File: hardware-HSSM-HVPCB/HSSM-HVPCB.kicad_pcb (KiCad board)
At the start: 2 copper layers, 66 parts, among them J1 2086-1103, J2 2601-1110, K1 G6DN-1A-L DC12, K2 G6DN-1A-L DC12, Q1 Q_NMOS_SOT-23_IRLML6344, Q2 Q_NMOS_SOT-23_IRLML6344, U1 LNK3204D-TL, U2 CS5480-INZ, U3 LTV-354T, U4 LTV-354T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

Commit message: [#6] Update step models
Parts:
- C2: footprint HSSM-HVPCB:C_Radial_D8_L14_P3.5 -> HSSM-HVPCB:860021374009
- C3: footprint HSSM-HVPCB:C_Radial_D5_L11_P2 -> HSSM-HVPCB:860020372006
- moved RV1 1.43 mm to (130.2, 122.5)
- moved J1 0.34 mm to (166.1, 108.7), turned to 0 degrees
- moved K1 0.17 mm to (155.1, 106.0)
- moved K2 0.17 mm to (155.1, 112.7)

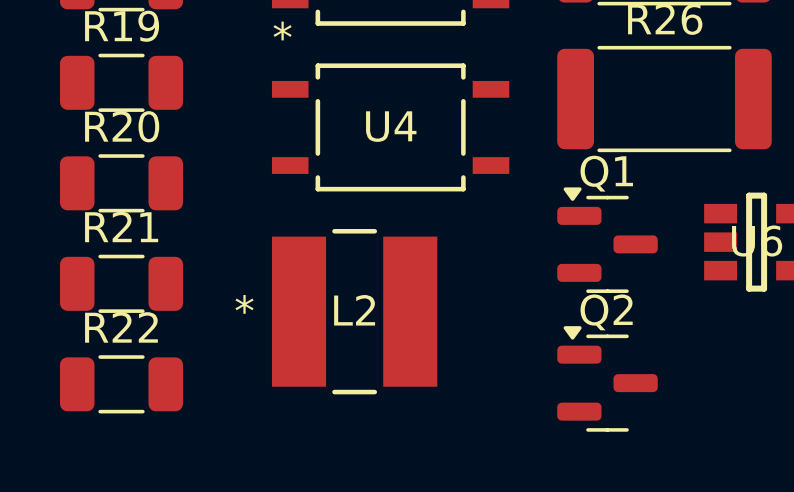
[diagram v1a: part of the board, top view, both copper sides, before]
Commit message: [#6] Add step model for SDR0503-102KL
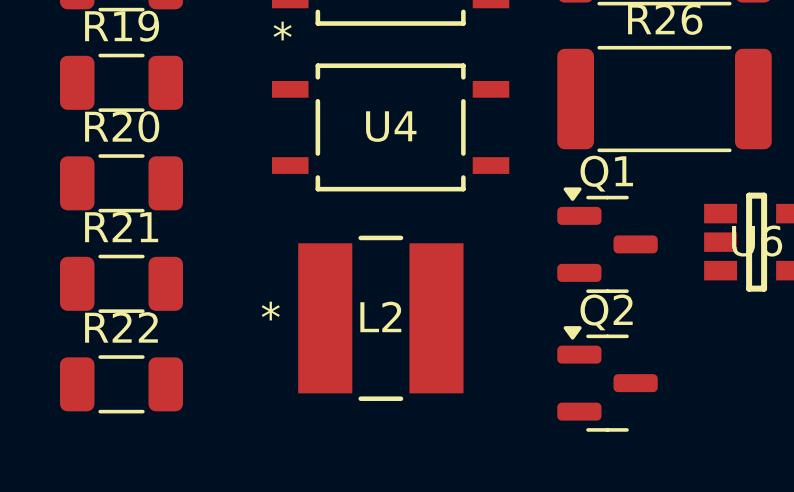
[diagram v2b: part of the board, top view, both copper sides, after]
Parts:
- moved L2 0.90 mm to (109.5, 135.9)

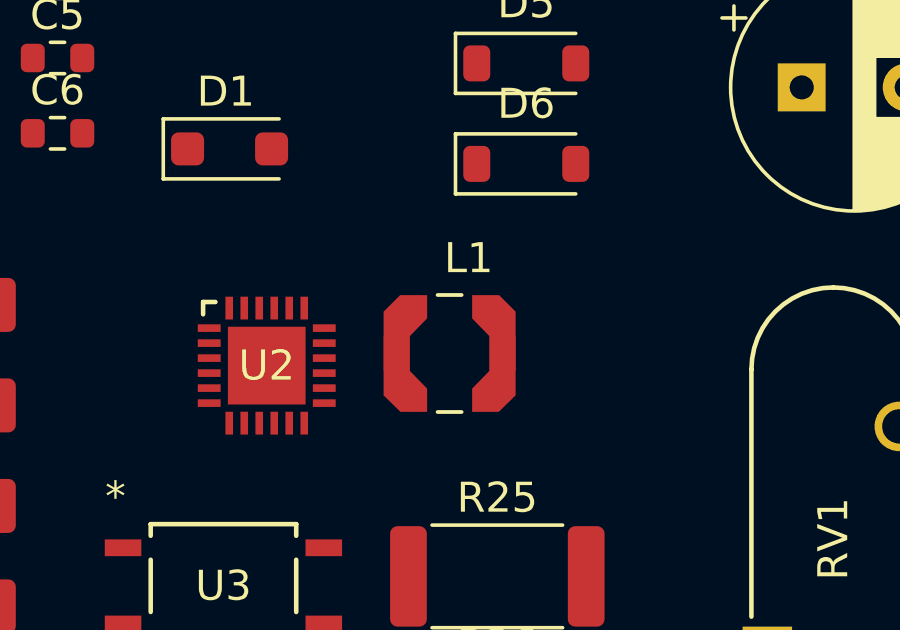
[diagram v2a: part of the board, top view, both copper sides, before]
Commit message: [#6] Add step model for LPS4012-155MRC
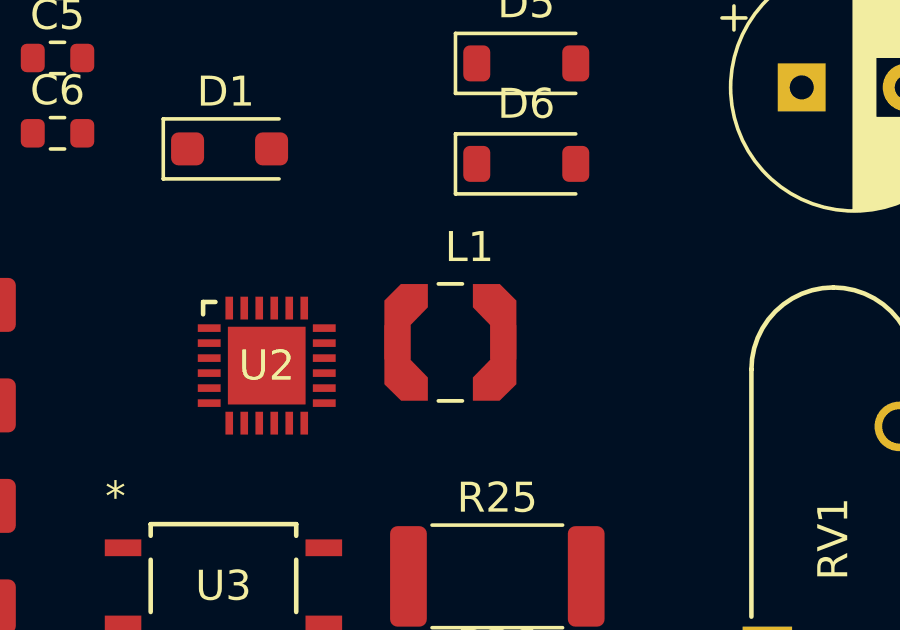
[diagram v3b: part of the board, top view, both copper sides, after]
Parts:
- moved L1 0.37 mm to (117.4, 115.9)

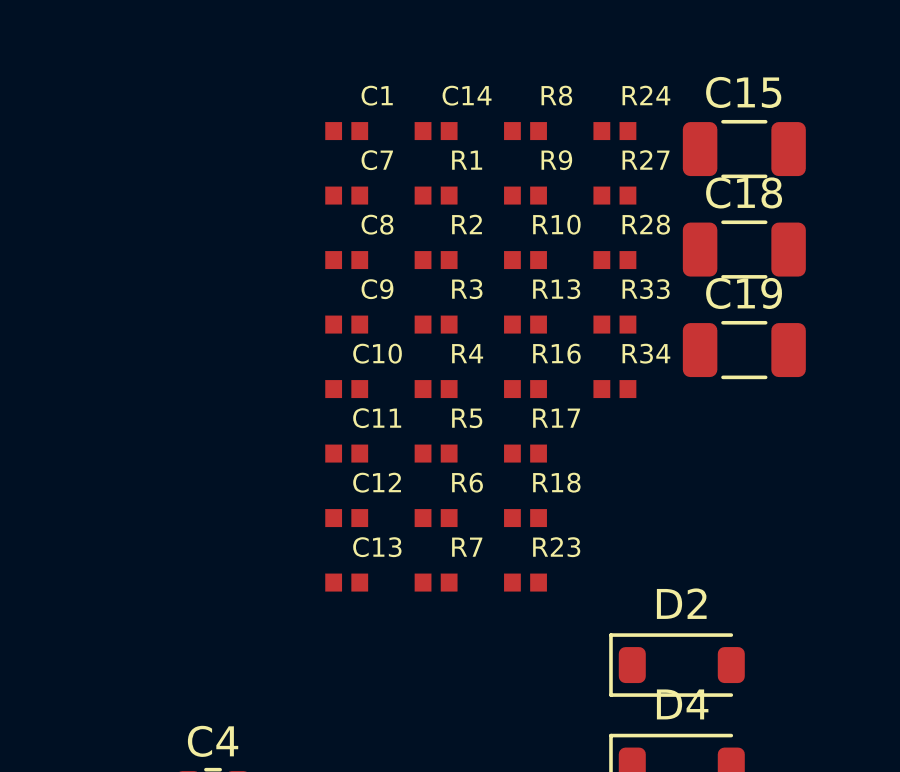
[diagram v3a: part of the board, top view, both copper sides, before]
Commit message: [#6] Add step model R_0402
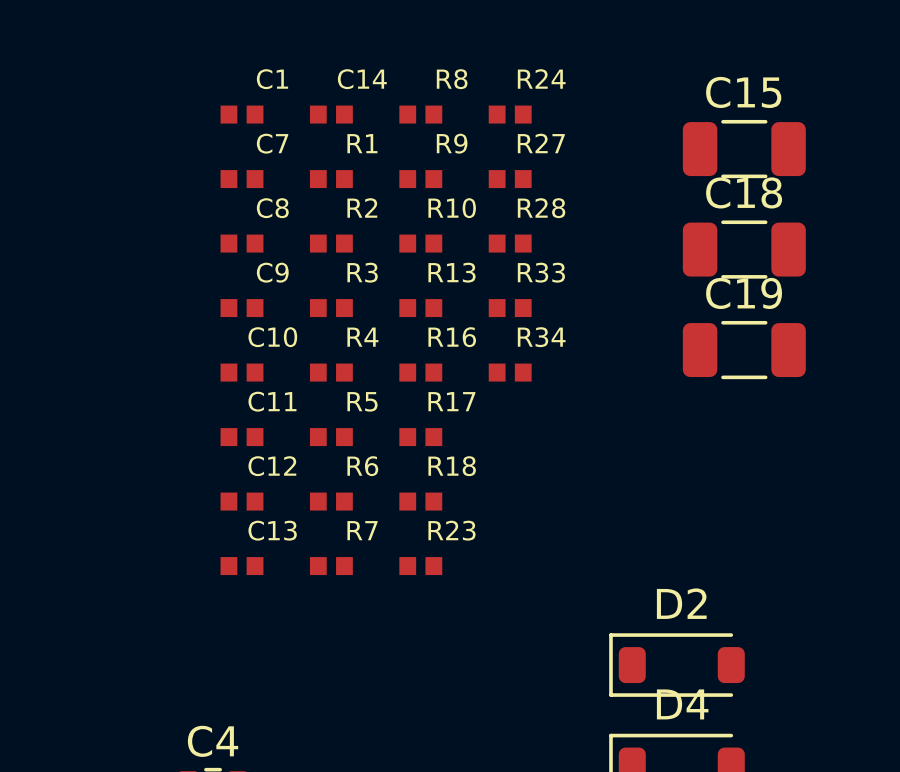
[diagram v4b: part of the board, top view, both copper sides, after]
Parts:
- moved R2 3.53 mm to (108.3, 85.8)
- moved R7 3.53 mm to (108.3, 96.6)
- moved C14 3.53 mm to (108.3, 81.5)
- moved R1 3.53 mm to (108.3, 83.7)
- moved R3 3.53 mm to (108.3, 88.0)
- moved R4 3.53 mm to (108.3, 90.2)
- moved R5 3.53 mm to (108.3, 92.3)
- moved R6 3.53 mm to (108.3, 94.5)
- moved C13 3.53 mm to (105.3, 96.6)
- moved C8 3.53 mm to (105.3, 85.8)
- moved R10 3.53 mm to (111.3, 85.8)
- moved R23 3.53 mm to (111.3, 96.6)
- moved R28 3.53 mm to (114.2, 85.8)
- moved C1 3.53 mm to (105.3, 81.5)
- moved C10 3.53 mm to (105.3, 90.2)
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
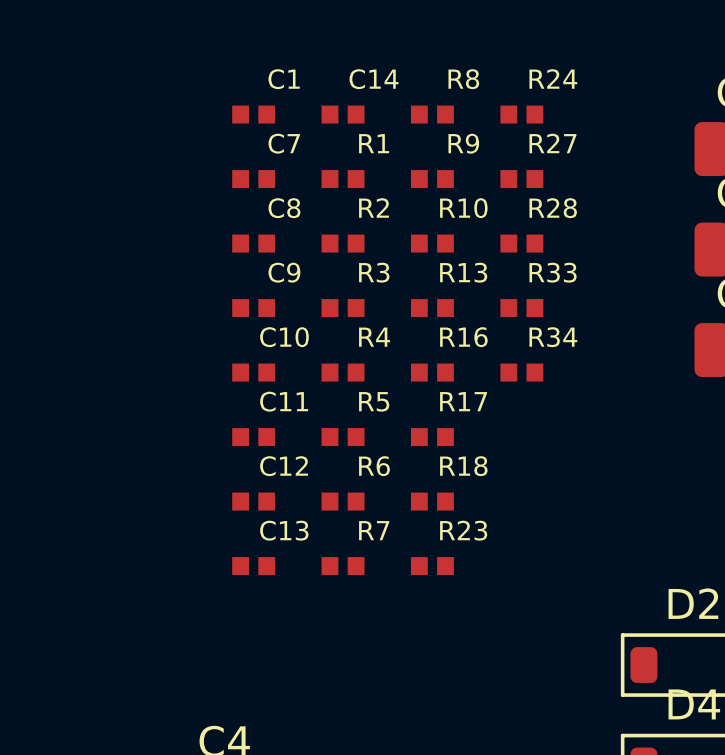
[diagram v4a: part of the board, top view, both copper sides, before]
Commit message: [#6] Add step model C_0402
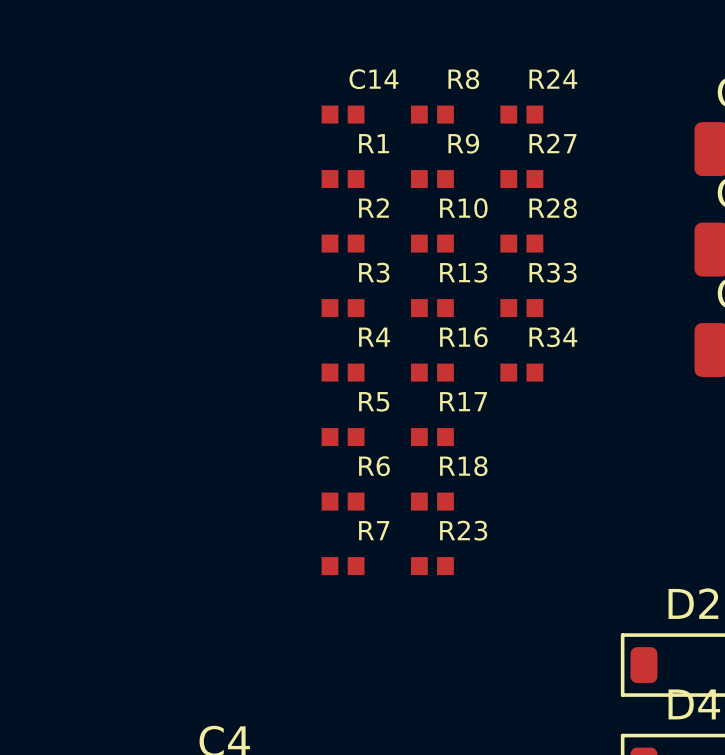
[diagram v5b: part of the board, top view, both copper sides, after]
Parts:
- removed C1: C_0u1_10pct_16V_0402_GRM155R71C104KA88J, HSSM-HVPCB:C_0402
- removed C10, C11, C12, C7, C8, C9: C_33nF_10pct_50V_0402_CC0402KRX7R9BB333, HSSM-HVPCB:C_0402
- removed C13: C_0u1_10pct_50V_0402_GRM155R71H104KE14D, HSSM-HVPCB:C_0402

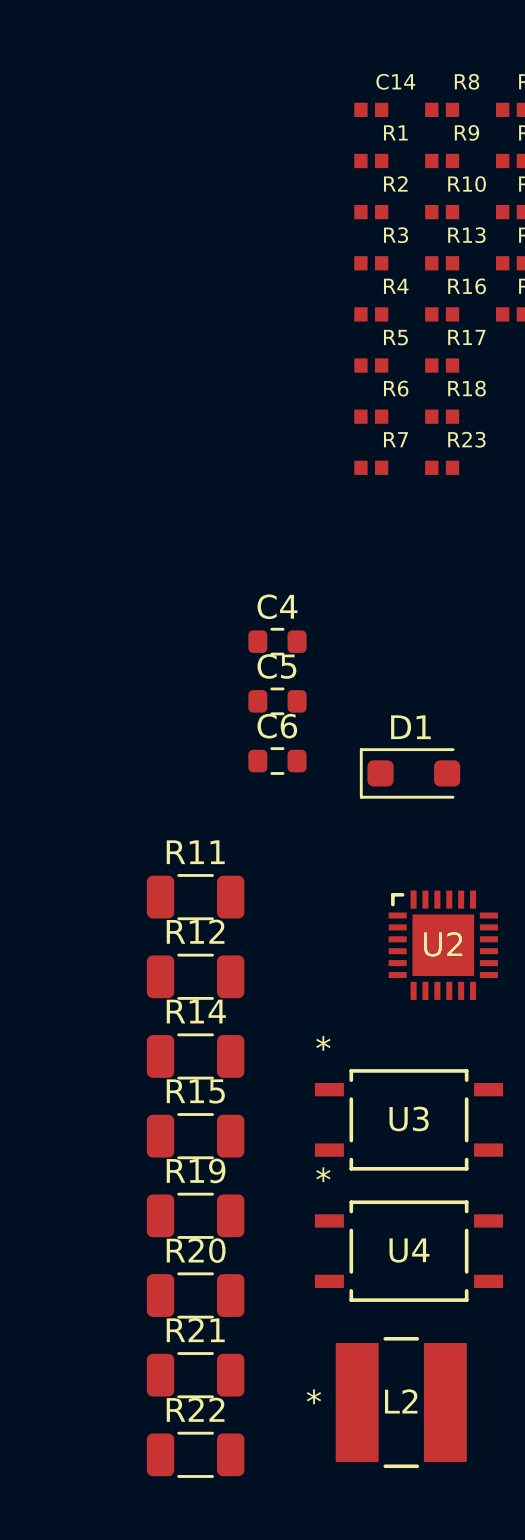
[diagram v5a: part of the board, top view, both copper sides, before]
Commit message: [#6] Fix step model R 1206
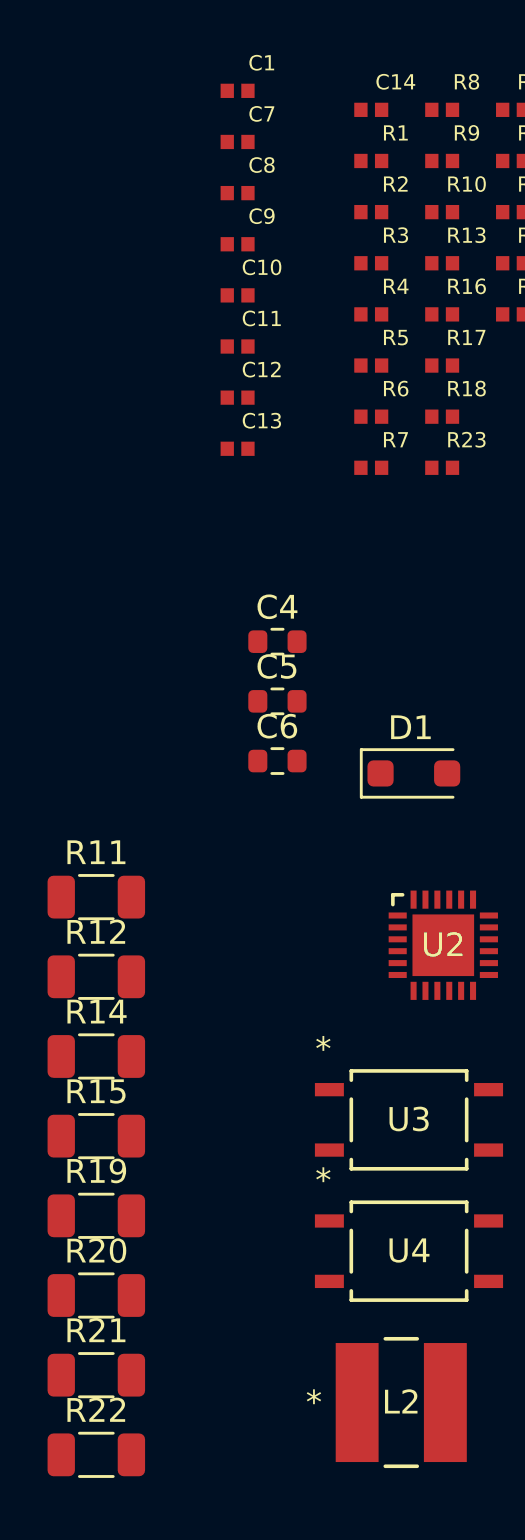
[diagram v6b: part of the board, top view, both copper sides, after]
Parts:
- added C1: C_0u1_10pct_16V_0402_GRM155R71C104KA88J, HSSM-HVPCB:C_0402, F.Cu at (102.7, 80.8)
- added C10: C_33nF_10pct_50V_0402_CC0402KRX7R9BB333, HSSM-HVPCB:C_0402, F.Cu at (102.7, 89.3)
- added C11: C_33nF_10pct_50V_0402_CC0402KRX7R9BB333, HSSM-HVPCB:C_0402, F.Cu at (102.7, 91.5)
- added C12: C_33nF_10pct_50V_0402_CC0402KRX7R9BB333, HSSM-HVPCB:C_0402, F.Cu at (102.7, 93.7)
- added C13: C_0u1_10pct_50V_0402_GRM155R71H104KE14D, HSSM-HVPCB:C_0402, F.Cu at (102.7, 95.8)
- added C7: C_33nF_10pct_50V_0402_CC0402KRX7R9BB333, HSSM-HVPCB:C_0402, F.Cu at (102.7, 82.9)
- added C8: C_33nF_10pct_50V_0402_CC0402KRX7R9BB333, HSSM-HVPCB:C_0402, F.Cu at (102.7, 85.0)
- added C9: C_33nF_10pct_50V_0402_CC0402KRX7R9BB333, HSSM-HVPCB:C_0402, F.Cu at (102.7, 87.2)
- moved R11 4.18 mm to (96.7, 114.7)
- moved R12 4.18 mm to (96.7, 118.0)
- moved R14 4.18 mm to (96.7, 121.3)
- moved R15 4.18 mm to (96.7, 124.7)
- moved R19 4.18 mm to (96.7, 128.1)
- moved R20 4.18 mm to (96.7, 131.4)
- moved R21 4.18 mm to (96.7, 134.8)
- moved R22 4.18 mm to (96.7, 138.1)

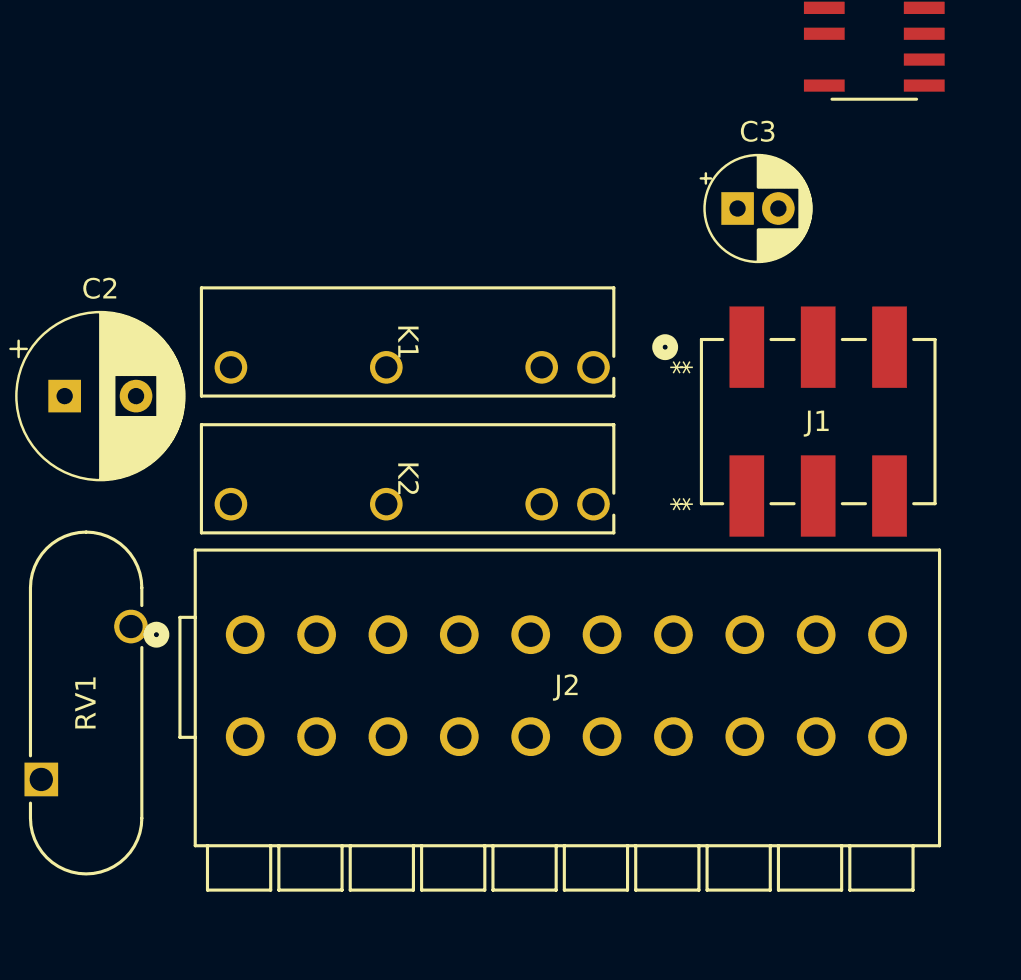
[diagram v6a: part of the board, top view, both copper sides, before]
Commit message: [#6] Add board outline
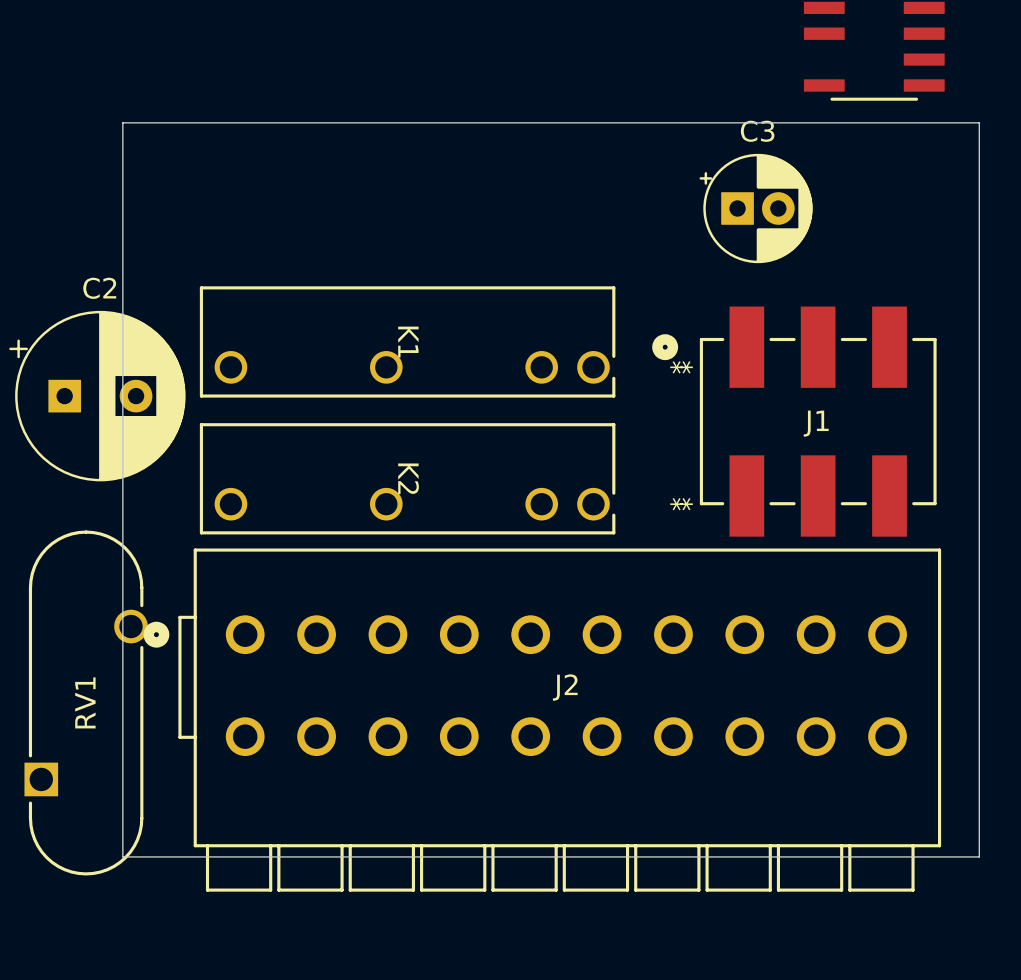
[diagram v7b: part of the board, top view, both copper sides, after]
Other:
- board outline added: 42 x 36 mm
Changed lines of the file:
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@@
 		)
 	)
+	(gr_rect
+		(start 132 94)
+		(end 174 130)
+		(stroke
+			(width 0.05)
+			(type default)
+		)
+		(fill none)
+		(layer "Edge.Cuts")
+	)
 )
